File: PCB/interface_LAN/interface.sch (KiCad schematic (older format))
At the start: 132 parts, among them J1 24VAC, J10 LIMIT12, J11 POT, J4 Power, J5 Control Signals, J6 HR913550A, J7 Sensor Feedback, J8 UART, J9 POT, Q1 8550, Q2 TIP127, Q3 MMBT5551, SW1 SW_SPST, SW2 CW, SW3 CCW, SW4 SET, U1 B1205-1W, U10 EL357, U11 74HCT595, U12 EL357, U13 AT24C64, U14 TL072, U15 HCNR201, U17 LMV358, U2 ESP32-WROOM-32, U3 LM317_TO-220, U4 L78L05_SOT89, U5 AMS1117-3.3, U6 OLED_128x32_4pin, U7 LAN8720A, U9 HCNR201

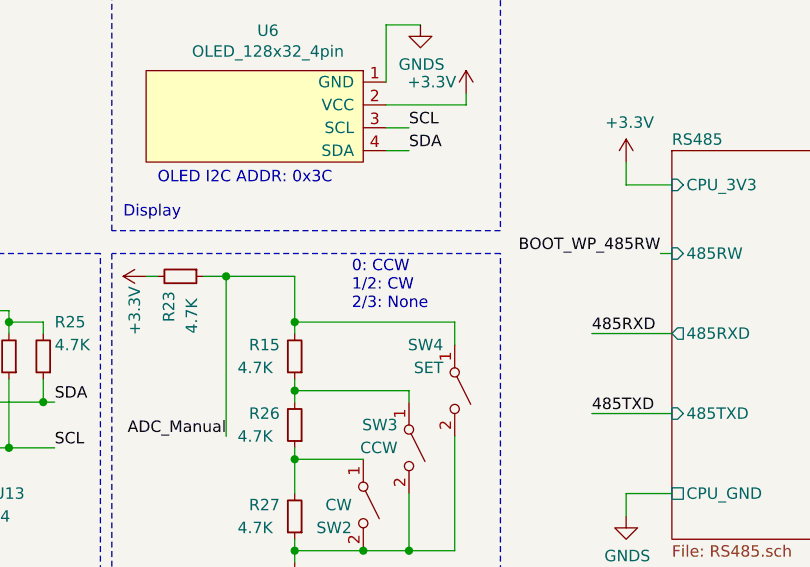
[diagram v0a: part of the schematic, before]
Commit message: Routed Interface_LAN MCU board
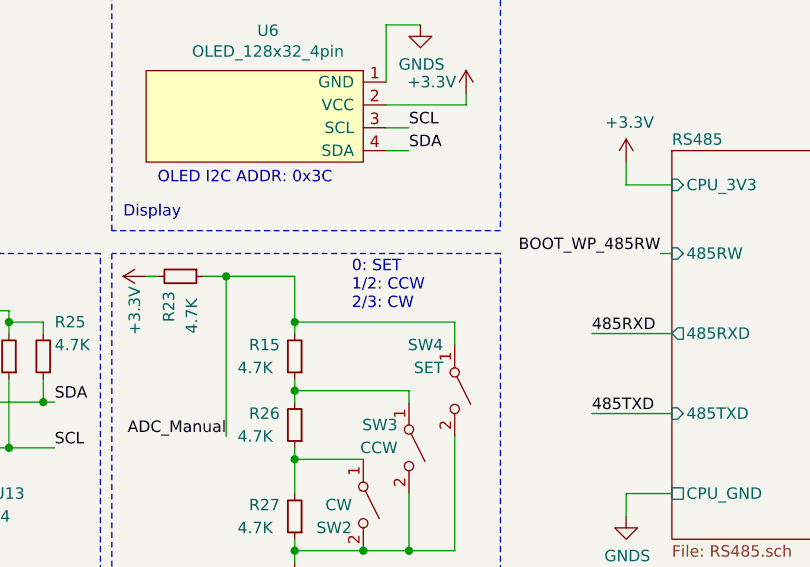
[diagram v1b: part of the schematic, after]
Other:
- note added: "0: SET\n1/2: CCW\n2/3: CW"
- note removed: "0: CCW\n1/2: CW\n2/3: None"
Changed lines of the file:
@@
 $EndComp
 Text Notes 6650 9550 0    50   ~ 0
-0: CCW\n1/2: CW\n2/3: None
+0: SET\n1/2: CCW\n2/3: CW
 Wire Wire Line
 	6100 10100 6100 9400

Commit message: Implemented the ESP-IDF version. First passed compilation
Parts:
- added C29, C39, C40: 104, lc_lib:0805_C, symbol Device:C_Small
- added J2: 0, lc_lib:1206_R, symbol Device:R_Small
- added J3: JTAG, Connector_PinHeader_2.54mm:PinHeader_1x04_P2.54mm_Vertical, symbol Connector_Generic:Conn_01x04
- C4: footprint (none) -> Connector_JST:JST_XH_B2B-XH-A_1x02_P2.50mm_Vertical
- D2: value 36V -> 50V
- R3: value 4.7K -> 100K
- R9: value 47K -> 10K
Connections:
- net +24V: now also J2.2
- net +3V3: no longer R3.2
- net ADC_Manual: now also U2.5 (SENSOR_VN), C29.1; no longer U2.23 (IO15)
- net GND: now also R3.2, C29.2, C39.2, C40.2
- net ISense1: now also U2.4 (SENSOR_VP); no longer U2.14 (IO12)
- net POT1: now also U2.6 (IO34), C40.1; no longer U2.4 (SENSOR_VP)
- net POT2: now also U2.7 (IO35), C39.1; no longer U2.5 (SENSOR_VN)
- net PROG_RXD: now also J8.2 (Pin_2), R18.2; no longer J8.3 (Pin_3), R19.2
- net PROG_TXD: now also J8.3 (Pin_3), R19.2; no longer J8.2 (Pin_2), R18.2
- net at C20.1, Q2.2 (C), U3.3 (VI): now also J2.1
- net BOOT_WP_485RW renamed BOOT_WP
- net LEDAX renamed LEDAX_485RW
- removed net LMTX1: R3.1, U10.4, U2.6 (IO34)
- net LMTX2 renamed LMTX2_TDO
- net LMTX2_TDO: now also R3.1, U2.23 (IO15), J3.2 (Pin_2); no longer U2.7 (IO35)
- net SPWM1 renamed SPWM1_TCK
- net SPWM1_TCK: now also J3.3 (Pin_3)
- net SPWM2 renamed SPWM2_TMS
- net SPWM2_TMS: now also J3.4 (Pin_4)
- new net LMTX1_TDI: J3.1 (Pin_1), U10.4, U2.14 (IO12)
- no-connect marks 7 -> 8
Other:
- note added: "ADC1_0"
- note added: "ADC1_3"
- note added: "ADC1_6"
- note added: "ADC1_7"
- note added: "BOOT2 PD"
- note added: "Cancel Log Out"
- note added: "IO34\35\nInput Only Pins"
- note added: "LOG PU(print) PD(cancel)"
- note added: "VDD_SDIO PD"
- moved on the sheet: C23, SC1, SC3

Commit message: motor control board with SPWM support`
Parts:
- removed C11: 104, lc_lib:0805_C, symbol Device:C_Small
- added C41: 104, lc_lib:0805_C, symbol Device:C_Small
- D1: symbol Diode:1N4007 -> MySchLib:D
- D4: symbol Device:D_Zener -> MySchLib:D_Zener
- R12: value 4.7K -> 22K
- R13: value 240 -> 860
- U14: value TL072 -> LM358
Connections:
- net +3V3: no longer J6.9 (LED_GA), R17.1
- net GND: now also J6.10 (LED_GK), C41.1
- net at C4.1, C5.1, C6.1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: now also D1.2 (K); no longer D1.1 (K)
- net at D2.1 (A1), F1.1: now also D1.1 (A); no longer D1.2 (A)
- net at R37.2, U15.6, U17.2 (-): now also C41.2
- net at R7.2, R8.1: now also D4.2 (K); no longer D4.1 (K)
- net at Q3.1 (B): now also D4.1 (A); no longer D4.2 (A)
- net at R36.1: now also J6.9 (LED_GA); no longer J6.10 (LED_GK)
- net at U7.15 (RST): now also R17.1; no longer R17.2
- net LMTX2_TDO renamed LMTX2_TDO_PHYRST
- net LMTX2_TDO_PHYRST: now also R17.2
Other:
- note added: "0: SET\n1/2: CCW\n2/3: CW\n3/4: None"
- note added: "OPAMP must be Ground Sensing"
- note added: "REGOFF=0: Use Internal 1.2V"
- note added: "nINTSEL=1 REFCLK in"
- note removed: "0: SET\n1/2: CCW\n2/3: CW"
- moved on the sheet: C14, C23, J4, J5, J7, R17, R33, R42

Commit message: Implenting SPWM
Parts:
- removed C15: 104, lc_lib:0805_C, symbol Device:C_Small
- removed R24, R25: 4.7K, lc_lib:0805_R, symbol Device:R_Small
- removed U13: AT24C64, lc_lib:SOIC-8_150MIL, symbol Memory_NVRAM:FM24C64B
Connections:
- net LMTX2_TDO_PHYRST: no longer R17.2
- net BOOT_WP renamed BOOT_PHYRST
- net BOOT_PHYRST: now also R17.2
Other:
- note removed: "EEPROM I2C ADDR: 0x00"
- moved on the sheet: R17
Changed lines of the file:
@@
 	3500 6650 3650 6650
 $Comp
-L Memory_NVRAM:FM24C64B U13
-U 1 1 5EADC6FE
-P 4700 10050
-F 0 "U13" H 5150 9750 50  0000 C CNN
-F 1 "AT24C64" H 5000 9650 50  0000 C CNN
-F 2 "lc_lib:SOIC-8_150MIL" H 4700 10050 50  0001 C CNN
-F 3 "http://www.cypress.com/file/41651/download" H 4500 10400 50  0001 C CNN
-	1    4700 10050
-	1    0    0    -1
-$EndComp
-Wire Wire Line
-	4300 9850 4250 9850
-Wire Wire Line
-	4250 9850 4250 9950
-Wire Wire Line
-	4250 10050 4300 10050
-Wire Wire Line
-	4300 9950 4250 9950
-Connection ~ 4250 9950
-Wire Wire Line
-	4250 9950 4250 10050
-$Comp
 L power:GNDS #PWR051
 U 1 1 5EC984F1
@@
 Wire Wire Line
 	2900 5400 2900 5500
-$Comp
-L power:GNDS #PWR057
-U 1 1 5ECC6BFA
-P 4100 9950
-F 0 "#PWR057" H 4100 9700 50  0001 C CNN
-F 1 "GNDS" H 4105 9777 50  0000 C CNN
-F 2 "" H 4100 9950 50  0001 C CNN
-F 3 "" H 4100 9950 50  0001 C CNN
-	1    4100 9950
-	1    0    0    -1
-$EndComp
-$Comp
-L power:+3.3V #PWR045
-U 1 1 5ED1282B
-P 4700 9500
-F 0 "#PWR045" H 4700 9350 50  0001 C CNN
-F 1 "+3.3V" H 4750 9650 50  0000 C CNN
-F 2 "" H 4700 9500 50  0001 C CNN
-F 3 "" H 4700 9500 50  0001 C CNN
-	1    4700 9500
-	1    0    0    -1
-$EndComp
-$Comp
-L Device:C_Small C15
-U 1 1 5ED83481
-P 4550 9550
-F 0 "C15" H 4642 9596 50  0000 L CNN
-F 1 "104" H 4642 9505 50  0000 L CNN
-F 2 "lc_lib:0805_C" H 4550 9550 50  0001 C CNN
-F 3 "~" H 4550 9550 50  0001 C CNN
-	1    4550 9550
-	0    -1   -1   0
-$EndComp
-$Comp
-L power:GNDS #PWR046
-U 1 1 5EDD67BE
-P 4400 9600
-F 0 "#PWR046" H 4400 9350 50  0001 C CNN
-F 1 "GNDS" H 4200 9550 50  0000 C CNN
-F 2 "" H 4400 9600 50  0001 C CNN
-F 3 "" H 4400 9600 50  0001 C CNN
-	1    4400 9600
-	1    0    0    -1
-$EndComp
-$Comp
-L power:GNDS #PWR059
-U 1 1 5EF7AA9E
-P 4700 10500
-F 0 "#PWR059" H 4700 10250 50  0001 C CNN
-F 1 "GNDS" H 4705 10327 50  0000 C CNN
-F 2 "" H 4700 10500 50  0001 C CNN
-F 3 "" H 4700 10500 50  0001 C CNN
-	1    4700 10500
-	1    0    0    -1
-$EndComp
-Wire Wire Line
-	4700 10500 4700 10450
-$Comp
-L Device:R_Small R24
-U 1 1 5F369165
-P 5150 9750
-F 0 "R24" H 5350 9600 50  0000 R CNN
-F 1 "4.7K" H 5350 9700 50  0000 R CNN
-F 2 "lc_lib:0805_R" H 5150 9750 50  0001 C CNN
-F 3 "~" H 5150 9750 50  0001 C CNN
-	1    5150 9750
-	-1   0    0    1
-$EndComp
-$Comp
-L Device:R_Small R25
-U 1 1 5F38615D
-P 5300 9750
-F 0 "R25" H 5250 9600 50  0000 R CNN
-F 1 "4.7K" H 5250 9700 50  0000 R CNN
-F 2 "lc_lib:0805_R" H 5300 9750 50  0001 C CNN
-F 3 "~" H 5300 9750 50  0001 C CNN
-	1    5300 9750
-	-1   0    0    1
-$EndComp
-Wire Wire Line
-	5100 9950 5300 9950
-Wire Wire Line
-	5300 9950 5300 9850
-Wire Wire Line
-	5150 9850 5150 10150
-Wire Wire Line
-	5150 10150 5100 10150
-Wire Wire Line
-	5150 10150 5350 10150
-Connection ~ 5150 10150
-Wire Wire Line
-	5300 9950 5350 9950
-Connection ~ 5300 9950
-Wire Wire Line
-	5150 9650 5150 9600
-Wire Wire Line
-	5150 9600 5300 9600
-Wire Wire Line
-	5300 9600 5300 9650
-Text Label 5350 10150 0    50   ~ 0
-SCL
-Text Label 5350 9950 0    50   ~ 0
-SDA
 Wire Wire Line
 	14350 8300 14300 8300
@@
 	1    0    0    -1
 $EndComp
-Wire Wire Line
-	4400 9600 4400 9550
-Wire Wire Line
-	4400 9550 4450 9550
-Wire Wire Line
-	4650 9550 4700 9550
-Connection ~ 4700 9550
-Wire Wire Line
-	4700 9550 4700 9650
-Wire Wire Line
-	4700 9500 4700 9550
 $Comp
 L Device:C_Small C6
@@
 	3300 1850 3300 1900
 Wire Wire Line
-	4250 9950 4100 9950
-Wire Wire Line
 	14050 8500 14300 8500
 Wire Wire Line
@@
 	1600 4500 1950 4500
 Text Label 3000 7000 2    50   ~ 0
-BOOT_WP
+BOOT_PHYRST
 $Comp
 L MySchLib:OLED_128x32_4pin U6
@@
 Wire Wire Line
 	6900 8750 6800 8750
-Text Notes 4250 10850 0    50   ~ 0
-EEPROM I2C ADDR: 0x00
 Text Notes 5800 9000 0    50   ~ 0
 OLED I2C ADDR: 0x3C
@@
 Text Label 4200 7400 0    50   ~ 0
 485RXD
-Wire Wire Line
-	4700 9550 5150 9550
-Wire Wire Line
-	5150 9550 5150 9600
-Connection ~ 5150 9600
 $Comp
 L power:GNDS #PWR0146
@@
 Text Notes 5650 9150 0    50   ~ 0
 Display
-Wire Notes Line
-	3950 9300 3950 10900
-Wire Notes Line
-	3950 10900 5550 10900
-Wire Notes Line
-	5550 10900 5550 9300
-Wire Notes Line
-	5550 9300 3950 9300
 NoConn ~ 6950 7000
 Text Notes 5950 6800 0    50   ~ 0
@@
 	1    0    0    -1
 $EndComp
-Text Label 4300 10250 2    50   ~ 0
-BOOT_WP
 $Comp
 L Device:R_Small R69
@@
 LMTX2_TDO_PHYRST
 Wire Wire Line
-	4900 8000 5150 8000
-Wire Wire Line
-	5500 8000 5500 6800
-Connection ~ 4900 8000
-Wire Wire Line
-	5350 8000 5500 8000
+	5500 8000 5500 7750
 Wire Wire Line
 	5950 6800 5950 6600
@@
 L Device:R_Small R?
 U 1 1 631AA6BF
-P 5250 8000
+P 5500 7650
 AR Path="/626CC43F/631AA6BF" Ref="R?"  Part="1"
 AR Path="/631AA6BF" Ref="R17"  Part="1"
-F 0 "R17" V 5150 8000 50  0000 C CNN
-F 1 "4.7K" V 5350 8000 50  0000 C CNN
-F 2 "lc_lib:0805_R" H 5250 8000 50  0001 C CNN
-F 3 "~" H 5250 8000 50  0001 C CNN
-	1    5250 8000
-	0    1    1    0
+F 0 "R17" V 5400 7650 50  0000 C CNN
+F 1 "4.7K" V 5600 7650 50  0000 C CNN
+F 2 "lc_lib:0805_R" H 5500 7650 50  0001 C CNN
+F 3 "~" H 5500 7650 50  0001 C CNN
+	1    5500 7650
+	1    0    0    -1
 $EndComp
 Text Label 12800 4250 0    50   ~ 0
@@
 Wire Wire Line
 	5500 6800 5950 6800
+Text Label 5500 8000 3    50   ~ 0
+BOOT_PHYRST
+Wire Wire Line
+	5500 6800 5500 7550
 $EndSCHEMATC
